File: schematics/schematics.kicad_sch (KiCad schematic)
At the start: 11 parts, among them Q1 S8050, Q2 S8050, U3 LM340AT

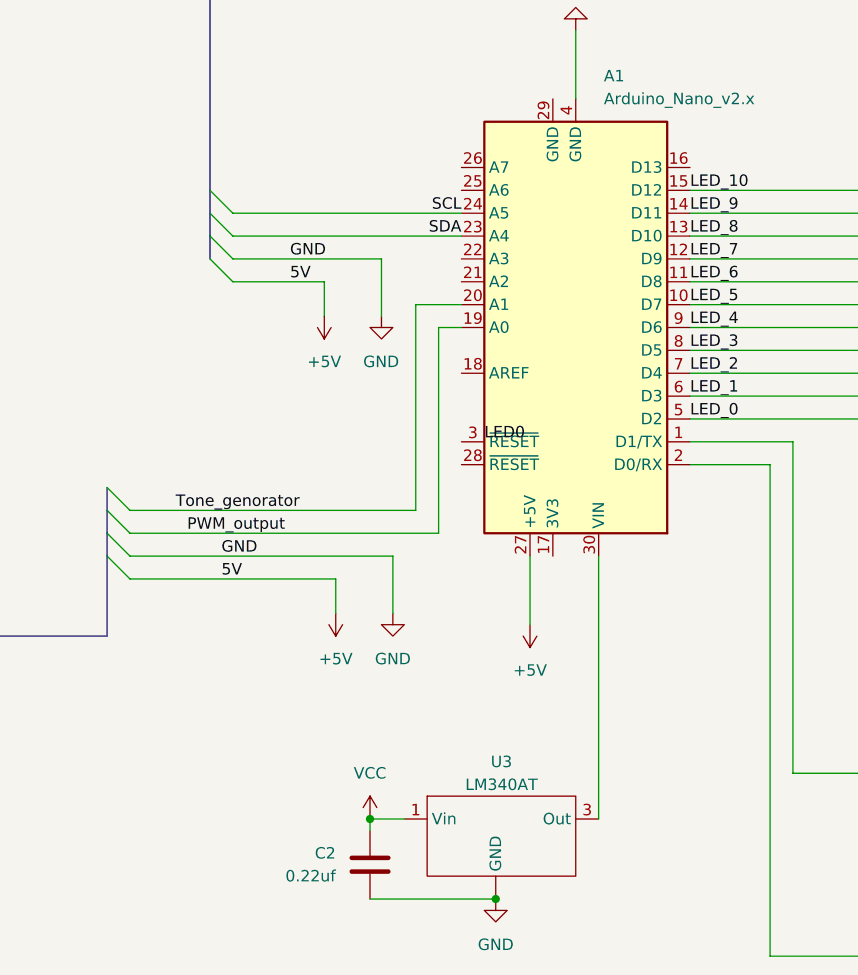
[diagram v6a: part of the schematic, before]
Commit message: changed voltage reg output from Vin to 5V to power arduino and added no connects to unused pins
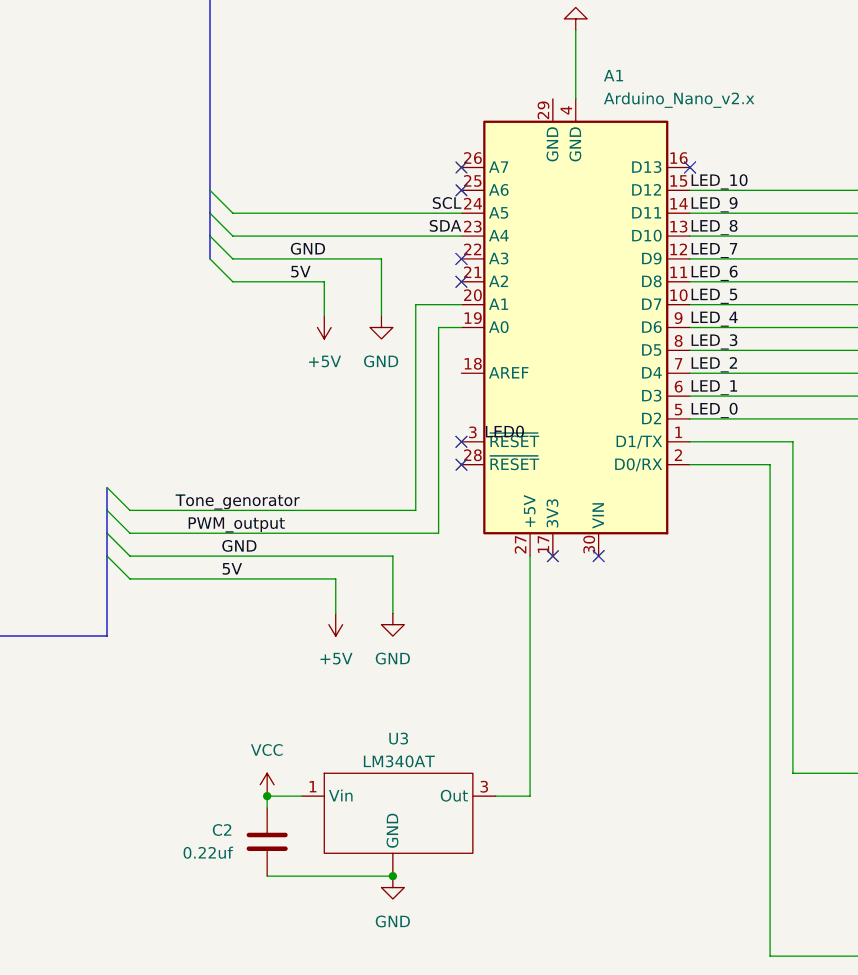
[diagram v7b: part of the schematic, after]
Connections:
- net +5V: no longer A1.27 (+5V)
- net at U3.3 (Out): now also A1.27 (+5V); no longer A1.30 (VIN)
- no-connect marks 0 -> 9
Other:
- moved on the sheet: C2, U3
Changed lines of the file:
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@@
 	)
 	(junction
-		(at 118.11 152.4)
+		(at 106.68 149.86)
 		(diameter 0)
 		(color 0 0 0 0)
@@
 	)
 	(junction
-		(at 132.08 161.29)
+		(at 120.65 158.75)
 		(diameter 0)
 		(color 0 0 0 0)
@@
 		(color 0 0 0 0)
 	)
+	(no_connect
+		(at 128.27 113.03)
+	)
+	(no_connect
+		(at 143.51 123.19)
+	)
+	(no_connect
+		(at 128.27 92.71)
+	)
+	(no_connect
+		(at 128.27 82.55)
+	)
+	(no_connect
+		(at 128.27 90.17)
+	)
+	(no_connect
+		(at 153.67 80.01)
+	)
+	(no_connect
+		(at 128.27 80.01)
+	)
+	(no_connect
+		(at 138.43 123.19)
+	)
+	(no_connect
+		(at 128.27 110.49)
+	)
 	(bus_entry
 		(at 180.34 92.71)
@@
 	(wire
 		(pts
+			(xy 132.08 149.86) (xy 135.89 149.86)
+		)
+		(stroke
+			(width 0)
+			(type default)
+		)
+	)
+	(wire
+		(pts
 			(xy 223.52 157.48) (xy 223.52 152.4)
 		)
@@
 		)
 	)
-	(wire
-		(pts
-			(xy 135.89 123.19) (xy 135.89 130.81)
-		)
-		(stroke
-			(width 0)
-			(type default)
-		)
-	)
-	(wire
-		(pts
-			(xy 143.51 152.4) (xy 143.51 123.19)
-		)
-		(stroke
-			(width 0)
-			(type default)
-		)
-	)
 	(bus
 		(pts
@@
 	(wire
 		(pts
-			(xy 118.11 161.29) (xy 132.08 161.29)
+			(xy 106.68 158.75) (xy 120.65 158.75)
 		)
 		(stroke
@@
 	(wire
 		(pts
+			(xy 135.89 149.86) (xy 135.89 123.19)
+		)
+		(stroke
+			(width 0)
+			(type default)
+		)
+	)
+	(wire
+		(pts
 			(xy 193.04 142.24) (xy 208.28 142.24)
 		)
@@
 	(wire
 		(pts
-			(xy 118.11 153.67) (xy 118.11 152.4)
+			(xy 106.68 151.13) (xy 106.68 149.86)
 		)
 		(stroke
@@
 	(wire
 		(pts
-			(xy 118.11 152.4) (xy 121.92 152.4)
+			(xy 106.68 149.86) (xy 110.49 149.86)
 		)
 		(stroke
@@
 	)
 	(symbol
-		(lib_id "power:+5V")
-		(at 135.89 130.81 180)
-		(unit 1)
-		(exclude_from_sim no)
-		(in_bom yes)
-		(on_board yes)
-		(dnp no)
-		(fields_autoplaced yes)
-		(property "Reference" "#PWR011"
-			(at 135.89 127 0)
-			(effects
-				(font
-					(size 1.27 1.27)
-				)
-				(hide yes)
-			)
-		)
-		(property "Value" "+5V"
-			(at 135.89 135.89 0)
-			(effects
-				(font
-					(size 1.27 1.27)
-				)
-			)
-		)
-		(property "Footprint" ""
-			(at 135.89 130.81 0)
-			(effects
-				(font
-					(size 1.27 1.27)
-				)
-				(hide yes)
-			)
-		)
-		(property "Datasheet" ""
-			(at 135.89 130.81 0)
-			(effects
-				(font
-					(size 1.27 1.27)
-				)
-				(hide yes)
-			)
-		)
-		(property "Description" "Power symbol creates a global label with name \"+5V\""
-			(at 135.89 130.81 0)
-			(effects
-				(font
-					(size 1.27 1.27)
-				)
-				(hide yes)
-			)
-		)
-		(pin "1"
-		)
-		(instances
-			(project ""
-				(path "/7fd7cdd6-b1c2-42a7-9276-fecd452b4132"
-					(reference "#PWR011")
-					(unit 1)
-				)
-			)
-		)
-	)
-	(symbol
 		(lib_id "Device:R_US")
 		(at 223.52 138.43 180)
@@
 	(symbol
 		(lib_id "Device:C")
-		(at 118.11 157.48 0)
+		(at 106.68 154.94 0)
 		(mirror y)
 		(unit 1)
@@
 		(dnp no)
 		(property "Reference" "C2"
-			(at 114.3 156.2099 0)
+			(at 102.87 153.6699 0)
 			(effects
 				(font
@@
 		)
 		(property "Value" "0.22uf"
-			(at 114.3 158.7499 0)
+			(at 102.87 156.2099 0)
 			(effects
 				(font
@@
 		)
 		(property "Footprint" ""
-			(at 117.1448 161.29 0)
+			(at 105.7148 158.75 0)
 			(effects
 				(font
@@
 		)
 		(property "Datasheet" "~"
-			(at 118.11 157.48 0)
+			(at 106.68 154.94 0)
 			(effects
 				(font
@@
 		)
 		(property "Description" "Unpolarized capacitor"
-			(at 118.11 157.48 0)
+			(at 106.68 154.94 0)
 			(effects
 				(font
@@
 	(symbol
 		(lib_id "power:VCC")
-		(at 118.11 152.4 0)
+		(at 106.68 149.86 0)
 		(unit 1)
 		(exclude_from_sim no)
@@
 		(fields_autoplaced yes)
 		(property "Reference" "#PWR021"
-			(at 118.11 156.21 0)
+			(at 106.68 153.67 0)
 			(effects
 				(font
@@
 		)
 		(property "Value" "VCC"
-			(at 118.11 147.32 0)
+			(at 106.68 144.78 0)
 			(effects
 				(font
@@
 		)
 		(property "Footprint" ""
-			(at 118.11 152.4 0)
+			(at 106.68 149.86 0)
 			(effects
 				(font
@@
 		)
 		(property "Datasheet" ""
-			(at 118.11 152.4 0)
+			(at 106.68 149.86 0)
 			(effects
 				(font
@@
 		)
 		(property "Description" "Power symbol creates a global label with name \"VCC\""
-			(at 118.11 152.4 0)
+			(at 106.68 149.86 0)
 			(effects
 				(font
@@
 	(symbol
 		(lib_id "power:GND")
-		(at 132.08 161.29 0)
+		(at 120.65 158.75 0)
 		(unit 1)
 		(exclude_from_sim no)
@@
 		(fields_autoplaced yes)
 		(property "Reference" "#PWR022"
-			(at 132.08 167.64 0)
+			(at 120.65 165.1 0)
 			(effects
 				(font
@@
 		)
 		(property "Value" "GND"
-			(at 132.08 166.37 0)
+			(at 120.65 163.83 0)
 			(effects
 				(font
@@
 		)
 		(property "Footprint" ""
-			(at 132.08 161.29 0)
+			(at 120.65 158.75 0)
 			(effects
 				(font
@@
 		)
 		(property "Datasheet" ""
-			(at 132.08 161.29 0)
+			(at 120.65 158.75 0)
 			(effects
 				(font
@@
 		)
 		(property "Description" "Power symbol creates a global label with name \"GND\" , ground"
-			(at 132.08 161.29 0)
+			(at 120.65 158.75 0)
 			(effects
 				(font
@@
 	(symbol
 		(lib_id "LM340AT:LM340AT")
-		(at 132.08 147.32 0)
+		(at 120.65 144.78 0)
 		(unit 1)
 		(exclude_from_sim no)
@@
 		(fields_autoplaced yes)
 		(property "Reference" "U3"
-			(at 132.715 146.05 0)
+			(at 121.285 143.51 0)
 			(effects
 				(font
@@
 		)
 		(property "Value" "LM340AT"
-			(at 132.715 148.59 0)
+			(at 121.285 146.05 0)
 			(effects
 				(font
@@
 		)
 		(property "Footprint" "Package_TO_SOT_THT:TO-220-3_Vertical"
-			(at 132.08 147.32 0)
+			(at 120.65 144.78 0)
 			(effects
 				(font
@@
 		)
 		(property "Datasheet" "https://www.alldatasheet.com/datasheet-pdf/view/223217/ESTEK/7805A.html"
-			(at 132.08 147.32 0)
+			(at 120.65 144.78 0)
 			(effects
 				(font
@@
 		)
 		(property "Description" "Voltage regulator, 5V, 1.5A,THT"
-			(at 132.08 147.32 0)
-			(effects
-				(font
+			(at 120.65 144.78 0)
+			(effects
+				(font
